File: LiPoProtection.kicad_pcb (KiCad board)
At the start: 2 copper layers, 50 x 50 mm, 51 parts, among them P1 CONN_01X05, P2 Load, P3 Supply, Q1 IRLML2502, U1 LM324, U2 LM324, U3 74HC08, U4 LP2950

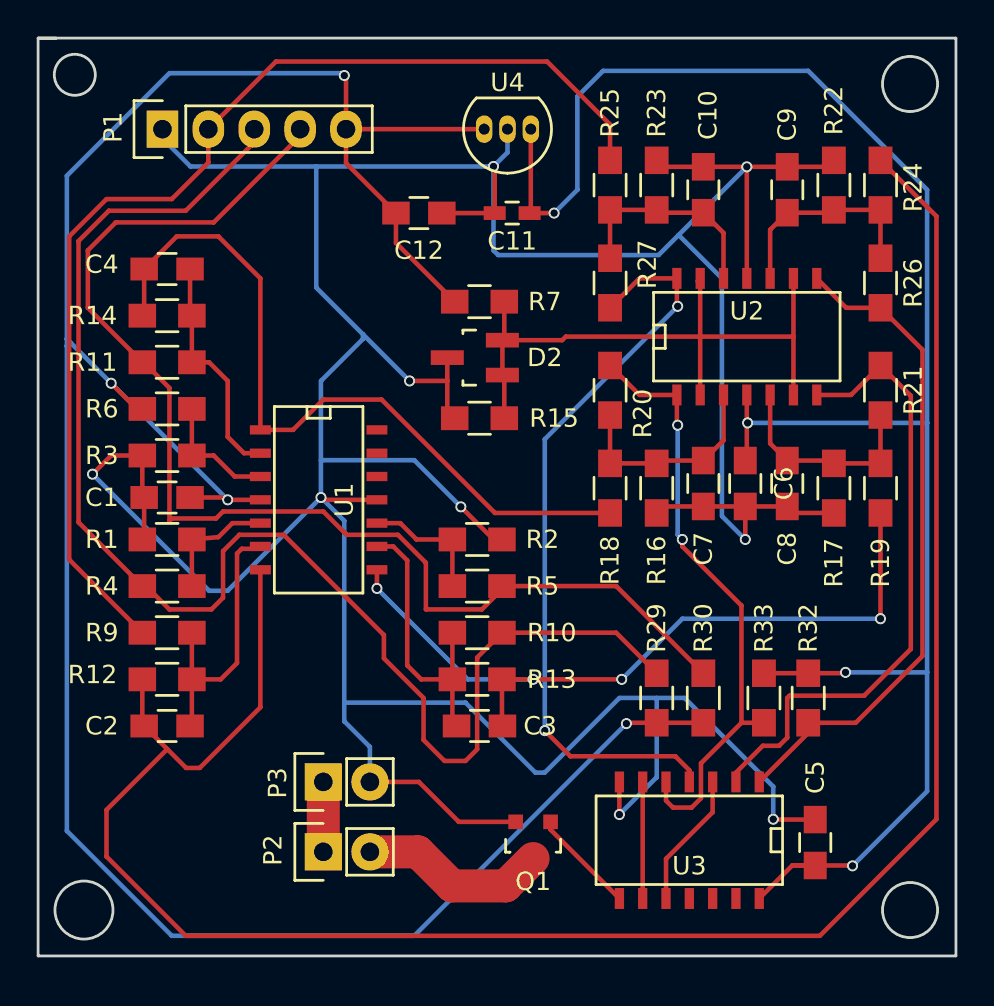
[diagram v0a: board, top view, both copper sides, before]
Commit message: Added libraries, added flyout diode
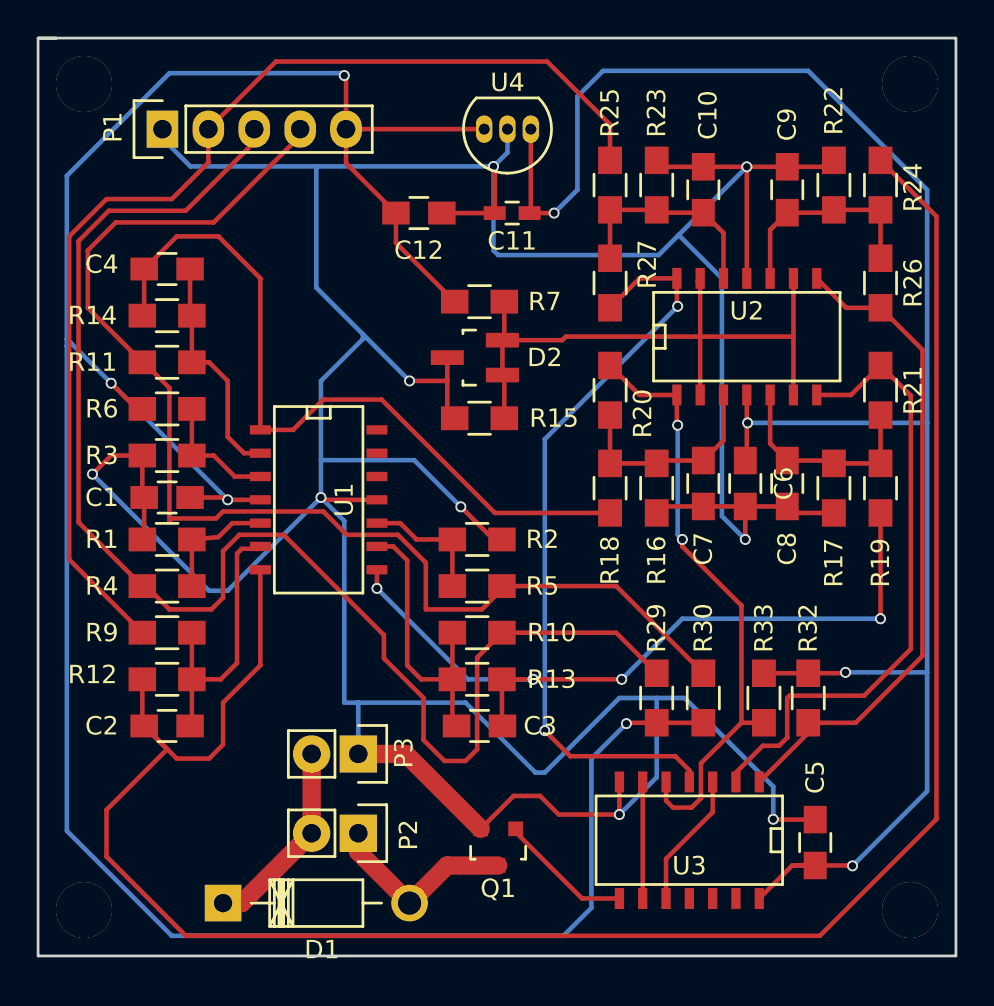
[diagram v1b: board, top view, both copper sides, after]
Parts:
- added D1: D, Diodes_ThroughHole:Diode_DO-41_SOD81_Horizontal_RM10, F.Cu at (100.1, 103.1)
- added REF**: MountingHole_3mm, Mounting_Holes:MountingHole_3mm, F.Cu at (137.5, 58.5)
- added REF**: MountingHole_3mm, Mounting_Holes:MountingHole_3mm, F.Cu at (137.5, 103.5)
- added REF**: MountingHole_3mm, Mounting_Holes:MountingHole_3mm, F.Cu at (92.5, 103.5)
- added REF**: MountingHole_3mm, Mounting_Holes:MountingHole_3mm, F.Cu at (92.5, 58.5)
- moved P3 2.44 mm to (107.4, 95.0), turned to 270 degrees
- moved P2 2.16 mm to (107.4, 99.3), turned to 270 degrees
- moved Q1 1.94 mm to (115.1, 100.1)
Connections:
- P2 pad 1: Net-(P2-Pad1) -> Net-(D1-Pad2)
- P2 pad 2: Net-(P2-Pad2) -> Net-(D1-Pad1)
- P3 pad 1: Net-(P2-Pad1) -> GND
- P3 pad 2: GND -> Net-(D1-Pad1)
- Q1 pad 3: Net-(P2-Pad2) -> Net-(D1-Pad2)
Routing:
- net Net-(D1-Pad1): track 0.00 -> 10.7 mm
- net Net-(D1-Pad2): track 0.00 -> 10.6 mm
- net Net-(P2-Pad2): track 10.3 -> 0.00 mm
- net GND: track 229.5 -> 235.7 mm
- net Net-(C1-Pad1): track 136.2 -> 140.9 mm
- net Net-(P2-Pad1): track 3.81 -> 0.00 mm
- net Net-(Q1-Pad1): track 5.73 -> 7.33 mm
- net Net-(C2-Pad1): track 112.7 -> 114.1 mm
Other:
- outline, holes or cut-outs redrawn

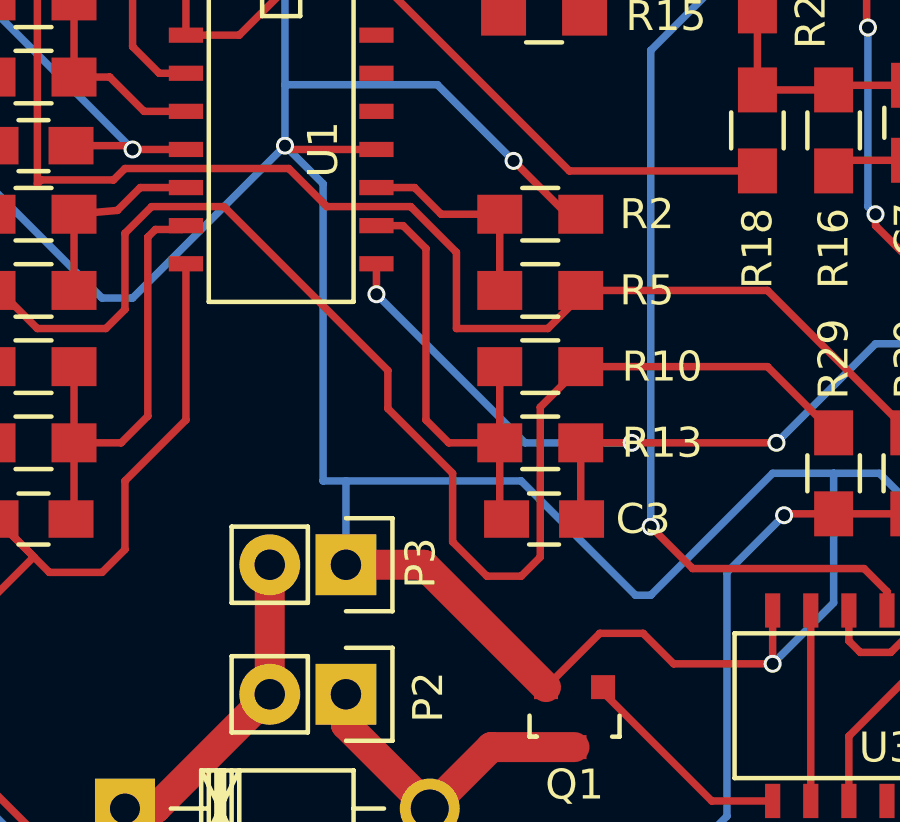
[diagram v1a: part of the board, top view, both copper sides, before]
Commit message: Added a view vias
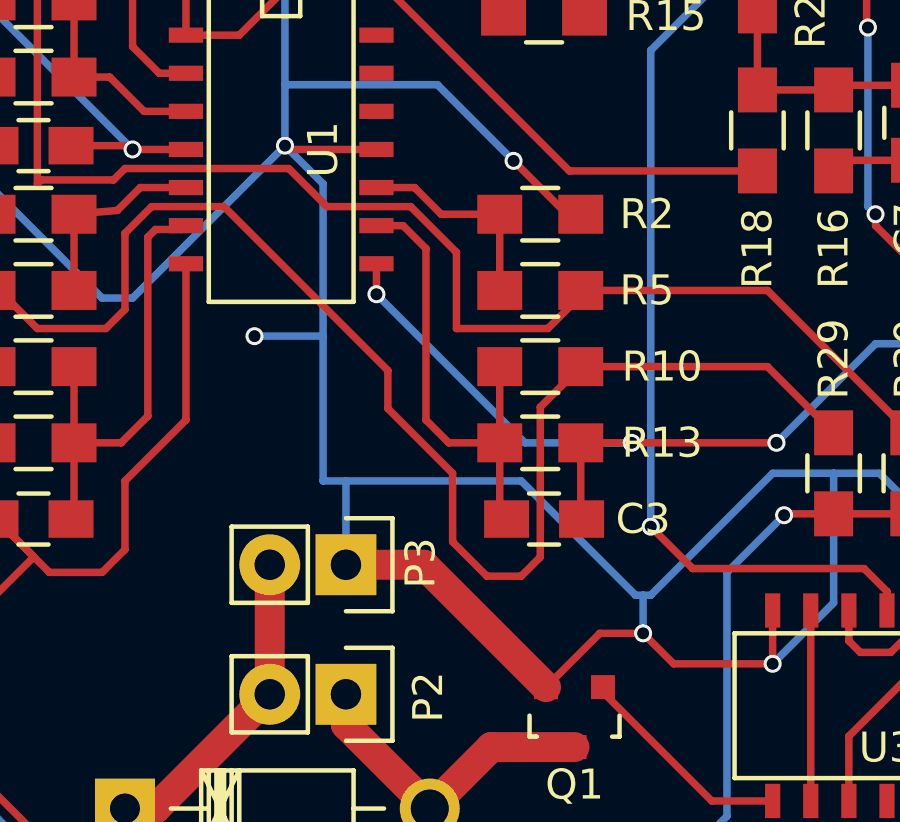
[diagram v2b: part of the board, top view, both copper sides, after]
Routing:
- net GND: track 235.7 -> 239.2 mm, vias 9 -> 11
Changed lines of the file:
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@@
     (links 111)
     (no_connects 0)
-    (area 89.924999 55.924999 140.075001 106.075001)
+    (area 70.000001 40.65 145.990046 109.47626)
     (thickness 1.6)
     (drawings 7)
-    (tracks 398)
+    (tracks 404)
     (zones 0)
     (modules 56)
@@
   )
   (setup
-    (last_trace_width 1)
+    (last_trace_width 0.25)
     (user_trace_width 1)
     (trace_clearance 0.2)
@@
     (arrow2b (pts (xy 78 56) (xy 78.586421 57.126504)))
   )
-  (segment (start 107.442 94.996) (end 110.03276 94.996) (width 1) (layer F.Cu) (net 1) (status 400000))
-  (segment (start 110.03276 94.996) (end 114.112 99.07524) (width 1) (layer F.Cu) (net 1) (status 800000))
-  (segment (start 107.442 92.202) (end 107.442 94.996) (width 0.25) (layer B.Cu) (net 1) (status 800000))
+  (segment (start 106.68 87.376) (end 104.394 87.376) (width 0.25) (layer B.Cu) (net 1))
+  (via (at 104.394 87.376) (size 0.6) (drill 0.4) (layers F.Cu B.Cu) (net 1))
+  (via (at 117.348 97.282) (size 0.6) (drill 0.4) (layers F.Cu B.Cu) (net 1))
+  (segment (start 117.348 97.282) (end 117.348 96.012) (width 0.25) (layer B.Cu) (net 1))
+  (segment (start 107.442 94.996) (end 110.03276 94.996) (width 1) (layer F.Cu) (net 1))
+  (segment (start 110.03276 94.996) (end 114.112 99.07524) (width 1) (layer F.Cu) (net 1))
+  (segment (start 107.442 92.202) (end 107.442 94.996) (width 0.25) (layer B.Cu) (net 1))
   (segment (start 121.666 98.298) (end 118.364 98.298) (width 0.25) (layer F.Cu) (net 1))
   (segment (start 118.364 98.298) (end 117.348 97.282) (width 0.25) (layer F.Cu) (net 1))
@@
   (segment (start 106.68 92.202) (end 107.442 92.202) (width 0.25) (layer B.Cu) (net 1))
   (segment (start 107.442 92.202) (end 113.284 92.202) (width 0.25) (layer B.Cu) (net 1))
+  (segment (start 117.094 96.012) (end 117.348 96.012) (width 0.25) (layer B.Cu) (net 1))
   (segment (start 113.284 92.202) (end 117.094 96.012) (width 0.25) (layer B.Cu) (net 1))
-  (segment (start 117.094 96.012) (end 117.602 96.012) (width 0.25) (layer B.Cu) (net 1))
+  (segment (start 117.348 96.012) (end 117.602 96.012) (width 0.25) (layer B.Cu) (net 1))
+  (segment (start 121.666 91.948) (end 123.698 91.948) (width 0.25) (layer B.Cu) (net 1))
   (segment (start 117.602 96.012) (end 121.666 91.948) (width 0.25) (layer B.Cu) (net 1))
-  (segment (start 121.666 91.948) (end 123.698 91.948) (width 0.25) (layer B.Cu) (net 1))
   (segment (start 123.698 91.948) (end 125.222 91.948) (width 0.25) (layer B.Cu) (net 1))
   (segment (start 125.222 91.948) (end 130.048 96.774) (width 0.25) (layer B.Cu) (net 1))
@@
   (segment (start 128.524 83.312) (end 128.524 81.514) (width 0.25) (layer F.Cu) (net 1))
   (segment (start 105.41 81.026) (end 106.68 82.296) (width 0.25) (layer B.Cu) (net 1))
-  (segment (start 106.68 82.296) (end 106.68 92.202) (width 0.25) (layer B.Cu) (net 1))
+  (segment (start 106.68 82.296) (end 106.68 87.376) (width 0.25) (layer B.Cu) (net 1))
+  (segment (start 106.68 87.376) (end 106.68 92.202) (width 0.25) (layer B.Cu) (net 1))
   (segment (start 95.778 81.026) (end 95.778 83.212) (width 0.25) (layer F.Cu) (net 1))
   (segment (start 95.778 83.212) (end 95.678 83.312) (width 0.25) (layer F.Cu) (net 1))
@@
   (segment (start 116.012 99.248) (end 116.012 99.07524) (width 0.25) (layer F.Cu) (net 26))
   (segment (start 122.936 102.87) (end 122.936 96.52) (width 0.25) (layer F.Cu) (net 27) (status 30))
-  (segment (start 115.062 101.07422) (end 112.28324 101.07422) (width 1) (layer F.Cu) (net 28) (status 400000))
-  (segment (start 112.28324 101.07422) (end 110.236 103.12146) (width 1) (layer F.Cu) (net 28) (status 800000))
-  (segment (start 107.442 99.314) (end 107.442 100.32746) (width 1) (layer F.Cu) (net 28) (status C00000))
-  (segment (start 107.442 100.32746) (end 110.236 103.12146) (width 1) (layer F.Cu) (net 28) (status C00000))
-  (segment (start 100.076 103.12146) (end 101.09454 103.12146) (width 1) (layer F.Cu) (net 29) (status 400000))
-  (segment (start 101.09454 103.12146) (end 104.902 99.314) (width 1) (layer F.Cu) (net 29) (status 800000))
-  (segment (start 104.902 99.314) (end 104.902 94.996) (width 1) (layer F.Cu) (net 29) (status C00000))
+  (segment (start 115.062 101.07422) (end 112.28324 101.07422) (width 1) (layer F.Cu) (net 28))
+  (segment (start 112.28324 101.07422) (end 110.236 103.12146) (width 1) (layer F.Cu) (net 28))
+  (segment (start 107.442 99.314) (end 107.442 100.32746) (width 1) (layer F.Cu) (net 28))
+  (segment (start 107.442 100.32746) (end 110.236 103.12146) (width 1) (layer F.Cu) (net 28))
+  (segment (start 100.076 103.12146) (end 101.09454 103.12146) (width 1) (layer F.Cu) (net 29))
+  (segment (start 101.09454 103.12146) (end 104.902 99.314) (width 1) (layer F.Cu) (net 29))
+  (segment (start 104.902 99.314) (end 104.902 94.996) (width 1) (layer F.Cu) (net 29))
   (zone (net 1) (net_name GND) (layer F.Cu) (hatch edge 0.508)
     (connect_pads (clearance 0.508))

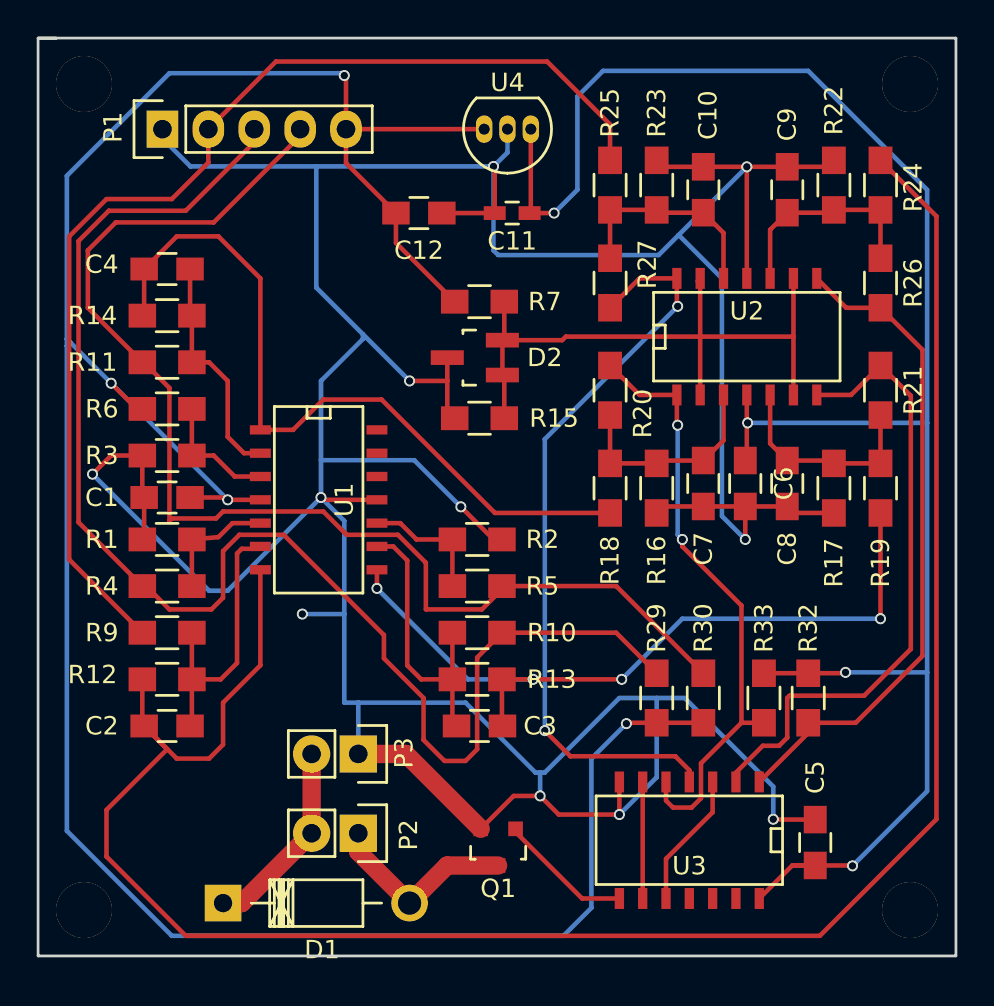
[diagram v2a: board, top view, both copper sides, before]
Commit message: Better trace placement
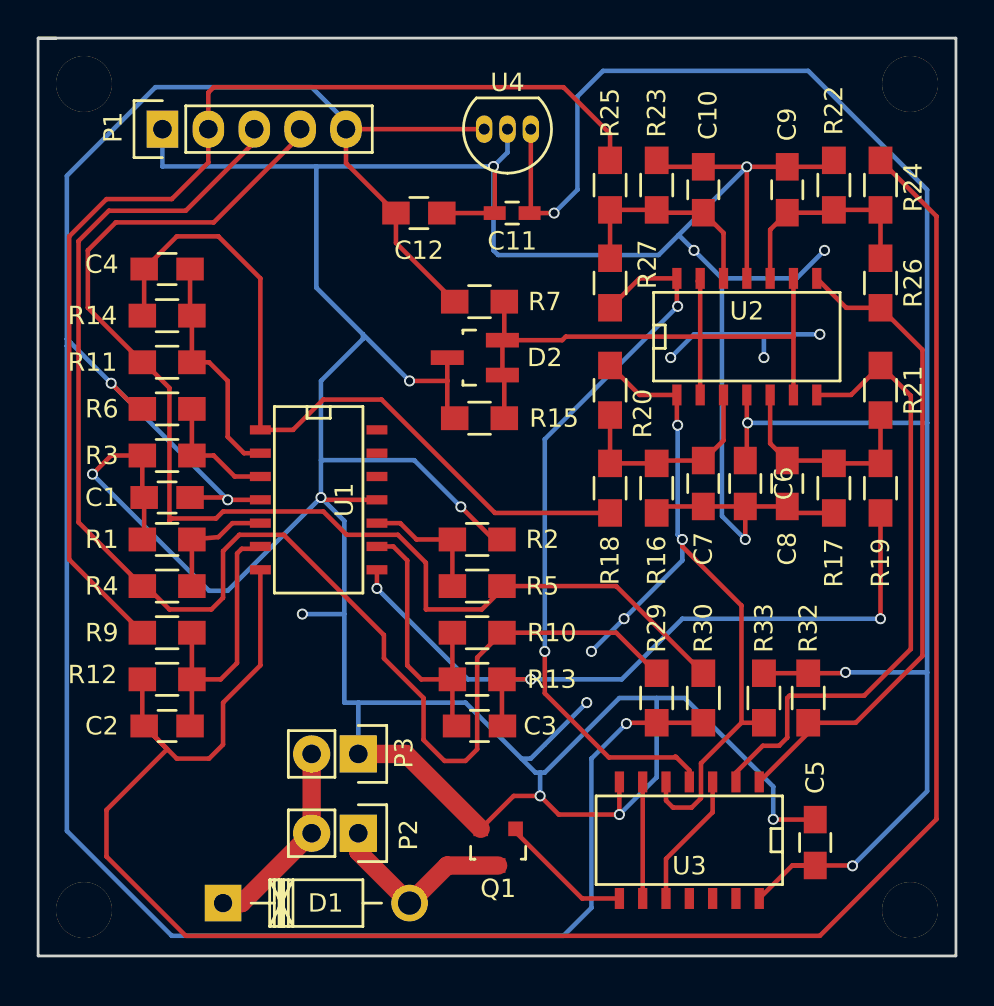
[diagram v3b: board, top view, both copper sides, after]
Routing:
- net GND: track 239.2 -> 261.6 mm, vias 11 -> 17
- net Net-(R20-Pad1): track 33.2 -> 41.3 mm, vias 2 -> 4
- net Net-(C1-Pad1): track 140.9 -> 138.9 mm, vias 4 -> 3
- net Net-(R27-Pad1): track 41.4 -> 40.3 mm
- net Net-(C3-Pad1): track 41.9 -> 41.8 mm, vias 4 -> 3

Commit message: Finishing touches, ordered.
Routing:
- net GND: track 261.6 -> 326.7 mm, vias 17 -> 27
- net Net-(R20-Pad1): track 41.3 -> 33.2 mm, vias 4 -> 2
- net Net-(C3-Pad1): track 41.8 -> 43.4 mm
